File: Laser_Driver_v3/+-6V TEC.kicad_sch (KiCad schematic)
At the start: 19 parts, among them U1 LM7808_TO220, U14 LT3045EDD 6V, U18 LT3094 -6V, U3 LM7908_TO220

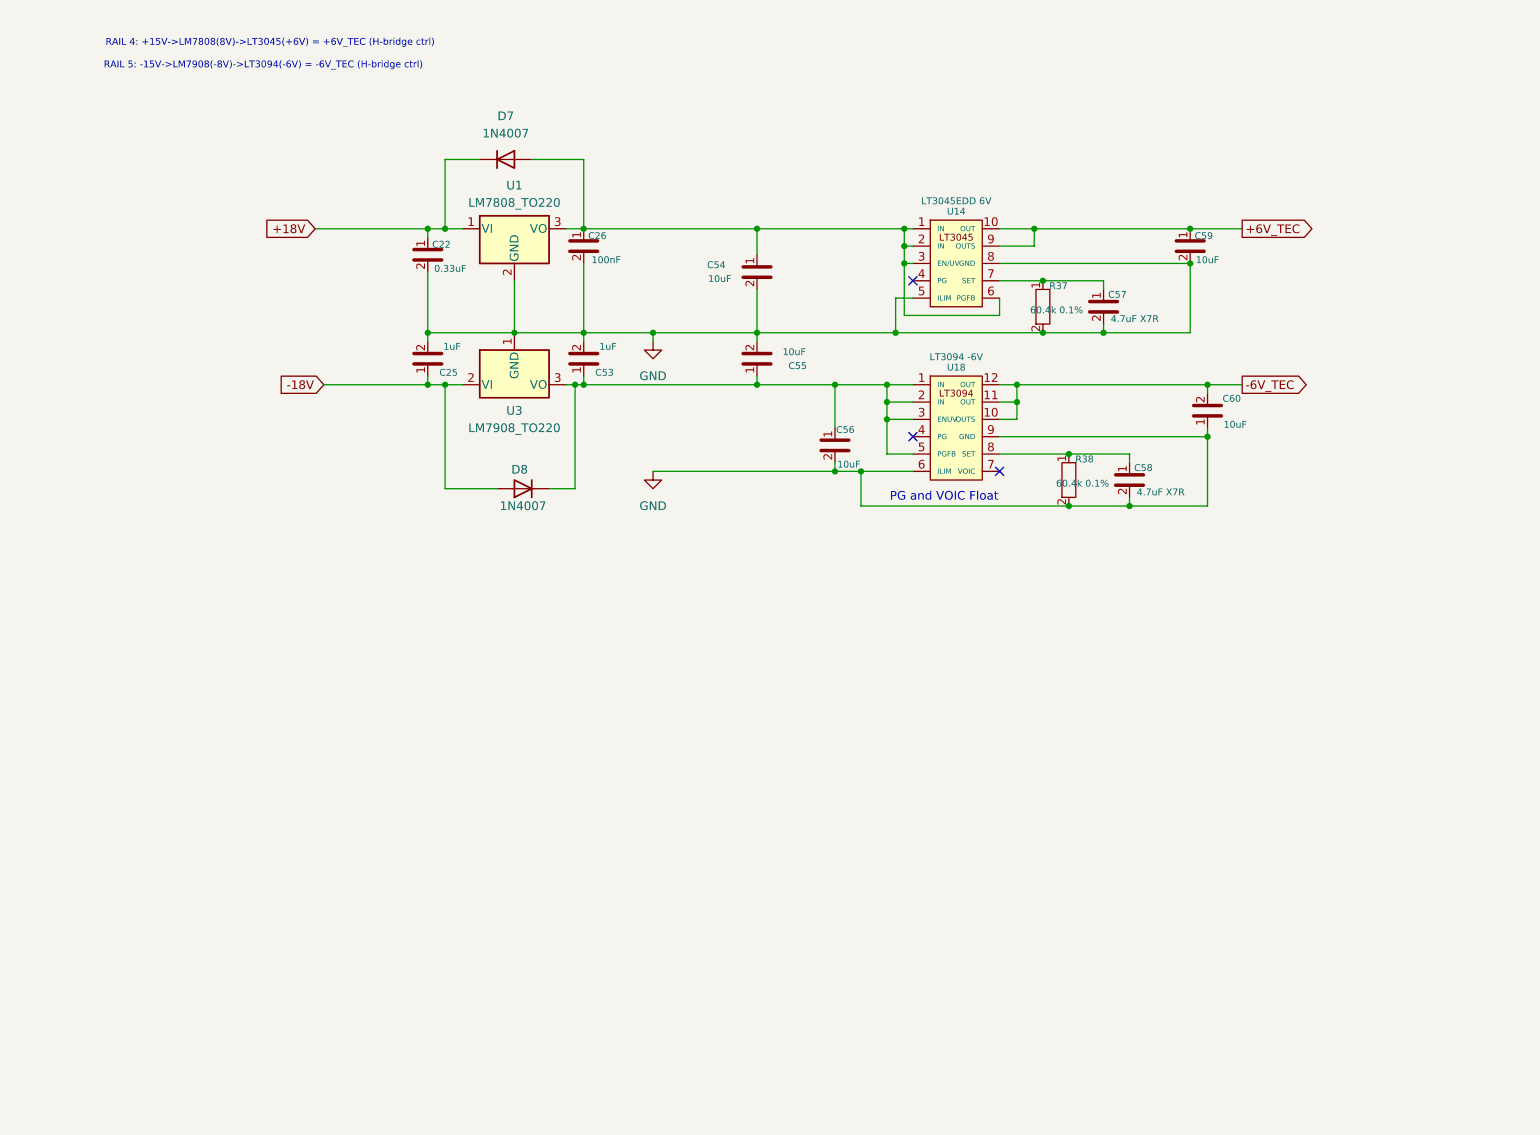
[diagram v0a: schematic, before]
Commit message: More updates for the power supply
H-bridge for TEC making sense.  +/-6V supply now making sense with capacitor multiplier good for 3A per polarity.
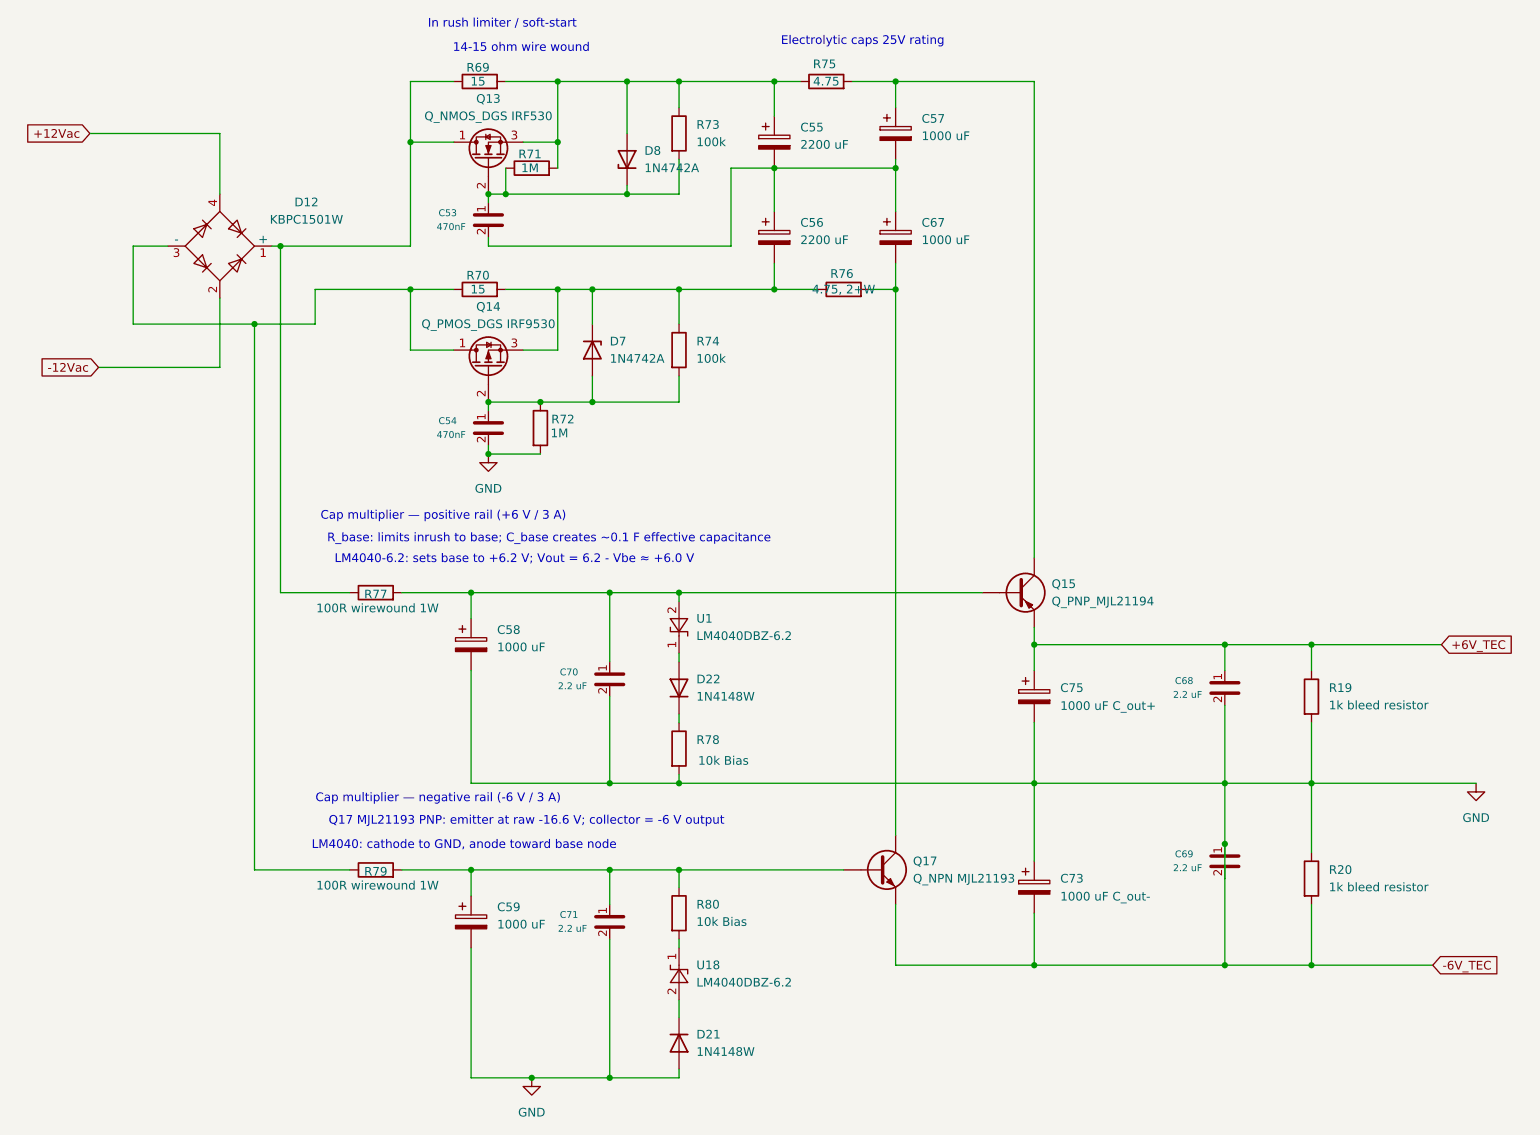
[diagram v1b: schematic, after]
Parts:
- removed C22: 0.33uF, Capacitor_SMD:C_0805_2012Metric_Pad1.18x1.45mm_HandSolder, symbol Device:C
- removed C25: 1uF, Capacitor_SMD:C_0805_2012Metric_Pad1.18x1.45mm_HandSolder, symbol Device:C
- removed C26: 100nF, Capacitor_SMD:C_0805_2012Metric_Pad1.18x1.45mm_HandSolder, symbol Device:C
- removed C55, C56, C59, C60: 10uF, Capacitor_SMD:C_0805_2012Metric_Pad1.18x1.45mm_HandSolder, symbol Device:C
- removed C57, C58: 4.7uF X7R, Capacitor_SMD:C_0805_2012Metric_Pad1.18x1.45mm_HandSolder, symbol Device:C
- removed D7, D8: 1N4007, Diode_THT:D_DO-41_SOD81_P10.16mm_Horizontal, symbol Diode:1N4007
- removed R37, R38: 60.4k 0.1%, Resistor_SMD:R_0402_1005Metric, symbol Device:R
- removed U1: LM7808_TO220, Package_TO_SOT_THT:TO-220-3_Vertical, symbol Regulator_Linear:LM7808_TO220
- removed U14: LT3045EDD 6V, Package_DFN_QFN:DFN-10-1EP_3x3mm_P0.5mm_EP1.65x2.38mm, symbol Regulator_Linear:LT3042
- removed U18: LT3094 -6V, Package_DFN_QFN:DFN-10-1EP_3x3mm_P0.5mm_EP1.65x2.38mm, symbol Regulator_Linear:LT3042
- removed U3: LM7908_TO220, Package_TO_SOT_THT:TO-220-3_Vertical, symbol Regulator_Linear:LM7908_TO220
- added C55, C56: 2200 uF, symbol Device:C_Polarized
- added C57, C58, C59, C67: 1000 uF, symbol Device:C_Polarized
- added C68, C69, C70, C71: 2.2 uF, Capacitor_SMD:C_0805_2012Metric_Pad1.18x1.45mm_HandSolder, symbol Device:C
- added C73: 1000 uF C_out-, Capacitor_THT:CP_Radial_D12.5mm_P5.00mm, symbol Device:C_Polarized
- added C75: 1000 uF C_out+, Capacitor_THT:CP_Radial_D12.5mm_P5.00mm, symbol Device:C_Polarized
- added D12: KBPC1501W, Diode_THT:Diode_Bridge_GeneSiC_KBPC_W, symbol Diode_Bridge:KBPC1501W
- added D21, D22: 1N4148W, Diode_SMD:D_SOD-123, symbol Diode:1N4148W
- added D7, D8: 1N4742A, Diode_THT:D_DO-41_SOD81_P10.16mm_Horizontal, symbol Diode:1N47xxA
- added Q13: Q_NMOS_DGS IRF530, symbol Transistor_FET:Q_NMOS_DGS
- added Q14: Q_PMOS_DGS IRF9530, symbol Transistor_FET:Q_PMOS_DGS
- added Q15: Q_PNP_MJL21194, Package_TO_SOT_THT:TO-264-3_Vertical, symbol Device:Q_PNP
- added Q17: Q_NPN MJL21193, Package_TO_SOT_THT:TO-264-3_Vertical, symbol Device:Q_NPN
- added R19, R20: 1k bleed resistor, Resistor_SMD:R_0805_2012Metric_Pad1.20x1.40mm_HandSolder, symbol Device:R
- added R69, R70: 15, symbol Device:R
- added R71, R72: 1M, symbol Device:R
- added R73, R74: 100k, symbol Device:R
- added R75: 4.75, symbol Device:R
- added R76: 4.75, 2+W, symbol Device:R
- added R77, R79: 100R wirewound 1W, symbol Device:R
- added R78, R80: 10k Bias, symbol Device:R
- added U1, U18: LM4040DBZ-6.2, Package_TO_SOT_SMD:SOT-23, symbol Reference_Voltage:LM4040DBZ-5
- C53: value 1uF -> 470nF
- C54: value 10uF -> 470nF
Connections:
- net +6V_TEC: now also C68.1, C75.1, Q15.E, R19.1
- net GND: now also C58.2, C59.2, C68.2, C69.1, C69.2, C70.2, C71.2, C73.1, C73.2, C75.2, D21.2 (A), Q17.E, R19.2, R20.1, R20.2, R72.2, R78.2; no longer C53.2
- net at C54.1: now also D7.2 (A), Q14.2 (G), R72.1, R74.2
- net at C53.1: now also D8.1 (K), Q13.2 (G), R71.1, R73.2
- new net: C53.2, C55.2, C56.1, C57.2, C67.1
- new net: D12.1 (+), Q13.1 (D), R69.1, R77.1
- new net: C58.1, C70.1, Q15.B, R77.2, U1.2 (A)
- new net: C59.1, C71.1, Q17.B, R79.2, R80.1
- new net: C56.2, D7.1 (K), Q14.3 (S), R70.2, R74.1, R76.1
- new net: D22.1 (K), R78.1
- new net: C55.1, D8.2 (A), Q13.3 (S), R69.2, R71.2, R73.1, R75.1
- new net: C67.2, Q17.C, R76.2
- new net: D22.2 (A), U1.1 (K)
- new net: D12.3 (-), Q14.1 (D), R70.1, R79.1
- new net: R80.2, U18.1 (K)
- new net: D21.1 (K), U18.2 (A)
- new net: C57.1, Q15.C, R75.2
- new net +12Vac: D12.4
- new net -12Vac: D12.2
- no-connect marks 3 -> 0
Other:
- note added: "14-15 ohm wire wound"
- note added: "Cap multiplier — negative rail (-6 V / 3 A)"
- note added: "Cap multiplier — positive rail (+6 V / 3 A)"
- note added: "Electrolytic caps 25V rating"
- note added: "In rush limiter / soft-start"
- note added: "LM4040-6.2: sets base to +6.2 V; Vout = 6.2 - Vbe ≈ +6.0 V"
- note added: "LM4040: cathode to GND, anode toward base node"
- note added: "Q17 MJL21193 PNP: emitter at raw -16.6 V; collector = -6 V output"
- note added: "R_base: limits inrush to base; C_base creates ~0.1 F effective capacitance"
- note removed: "PG and VOIC Float"
- note removed: "RAIL 4: +15V->LM7808(8V)->LT3045(+6V) = +6V_TEC (H-bridge ctrl)"
- note removed: "RAIL 5: -15V->LM7908(-8V)->LT3094(-6V) = -6V_TEC (H-bridge ctrl)"

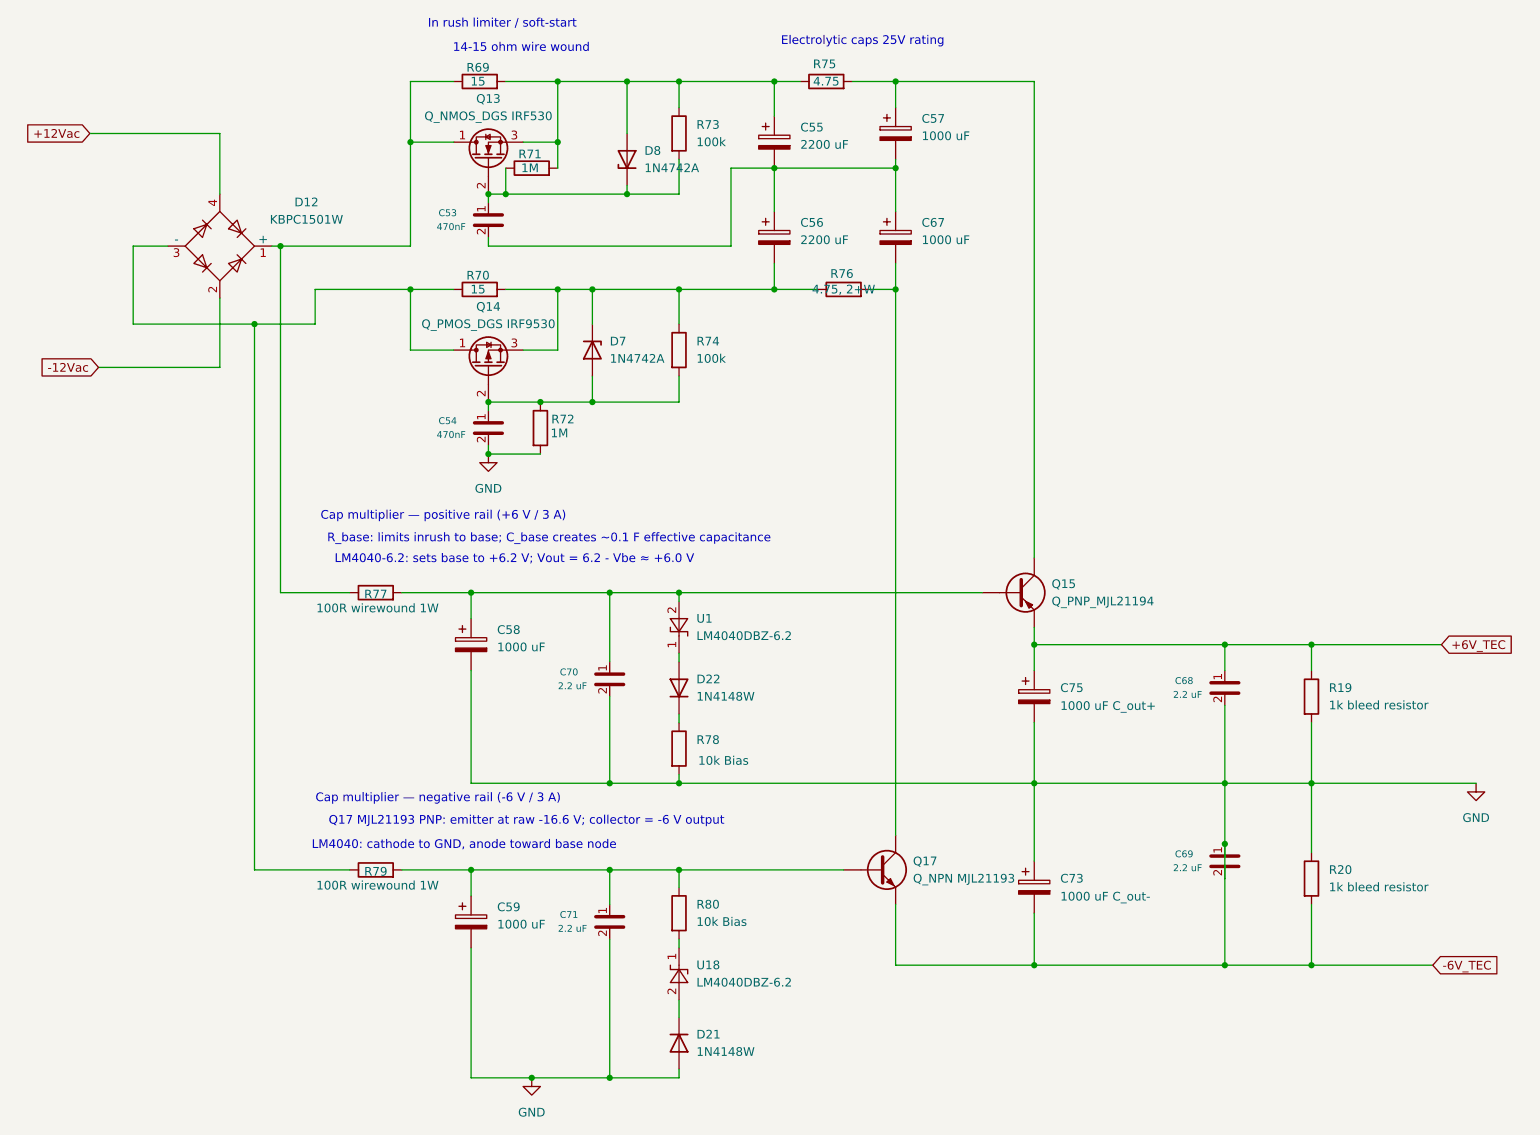
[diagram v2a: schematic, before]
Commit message: Renumbered schematics, corrections, power verified
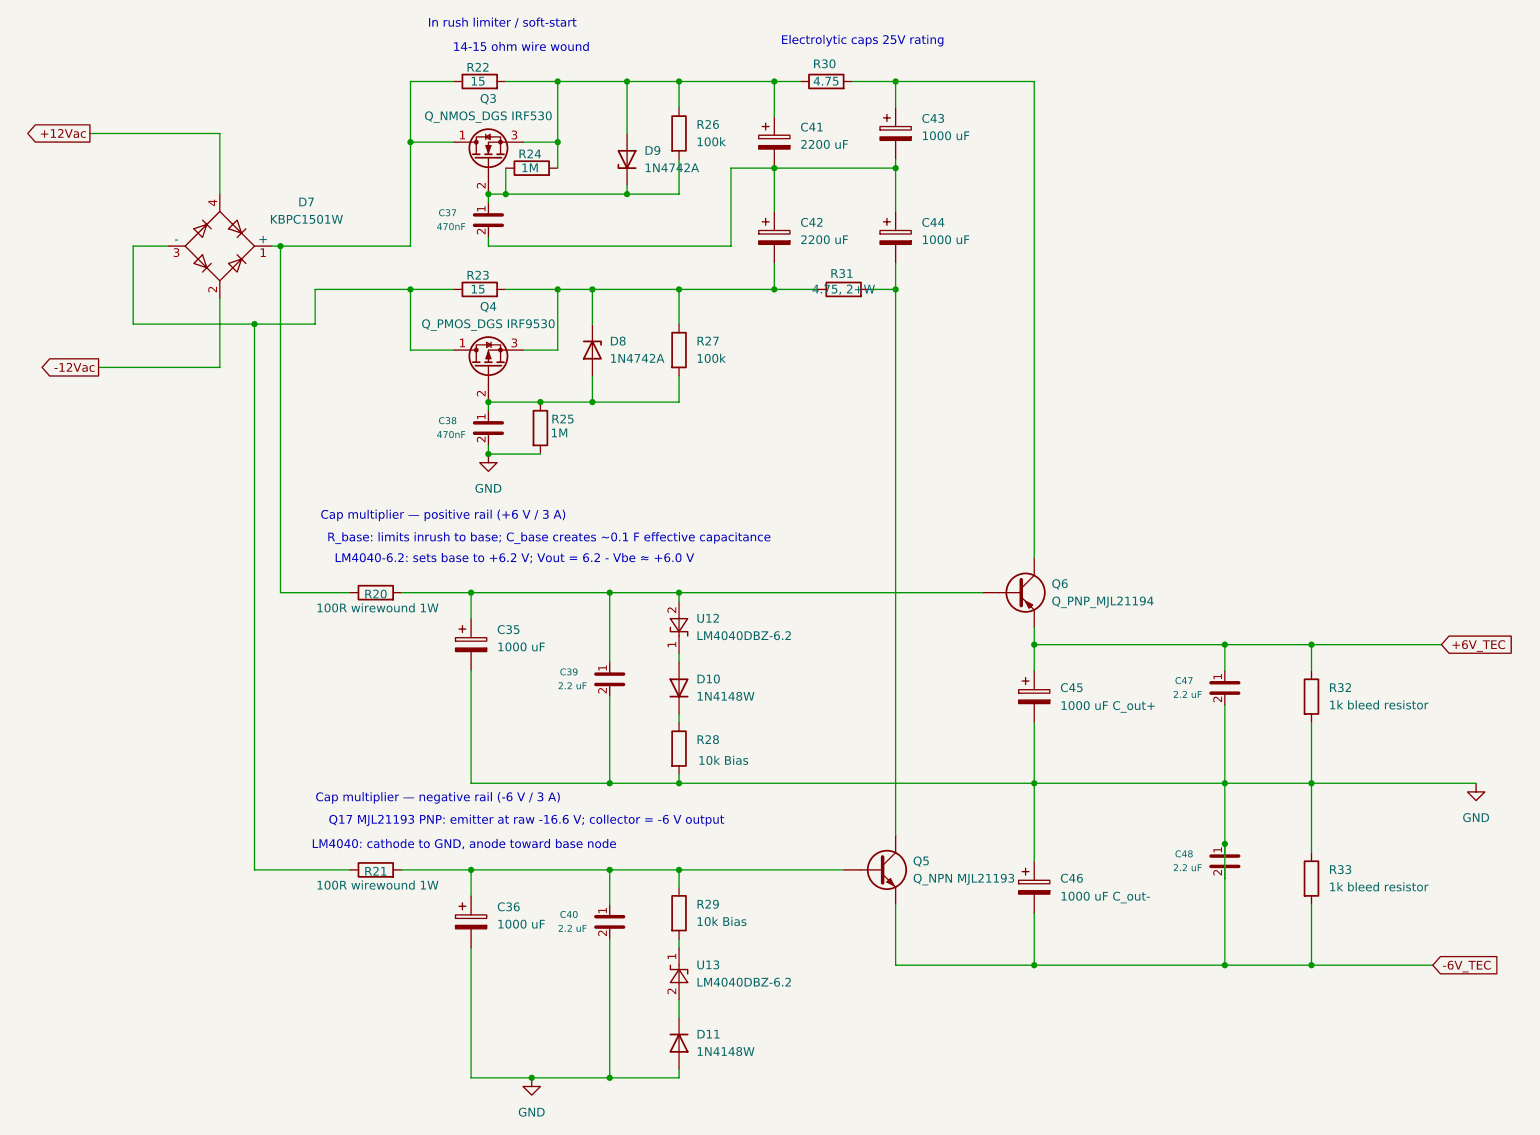
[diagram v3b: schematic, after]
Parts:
- renumbered C58 to C35, C59 to C36, C53 to C37, C54 to C38, C70 to C39, C71 to C40, C55 to C41, C56 to C42, C57 to C43, C67 to C44, C75 to C45, C73 to C46, C68 to C47, C69 to C48, D22 to D10, D21 to D11, D12 to D7, D7 to D8, D8 to D9, Q13 to Q3, Q14 to Q4, Q17 to Q5, Q15 to Q6, R77 to R20, R79 to R21, R69 to R22, R70 to R23, R71 to R24, R72 to R25, R73 to R26, R74 to R27, R78 to R28, R80 to R29, R75 to R30, R76 to R31, R19 to R32, R20 to R33, U1 to U12, U18 to U13
